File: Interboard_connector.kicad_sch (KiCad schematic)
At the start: 2 parts, among them J1 Chainbus Out, J4 Chainbus In

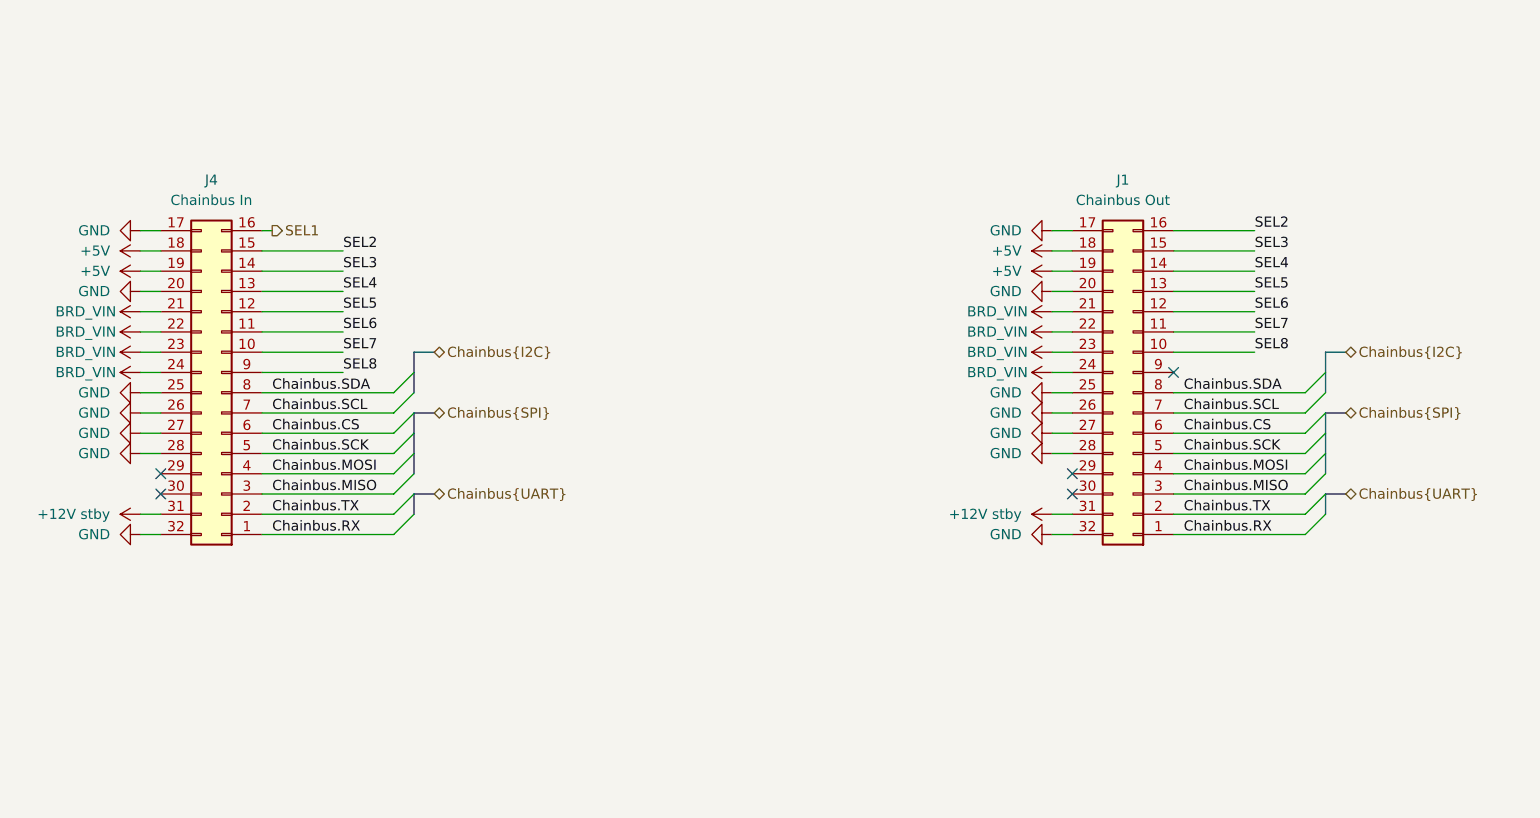
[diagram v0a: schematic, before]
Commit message: finished schematic (without some part numbers)
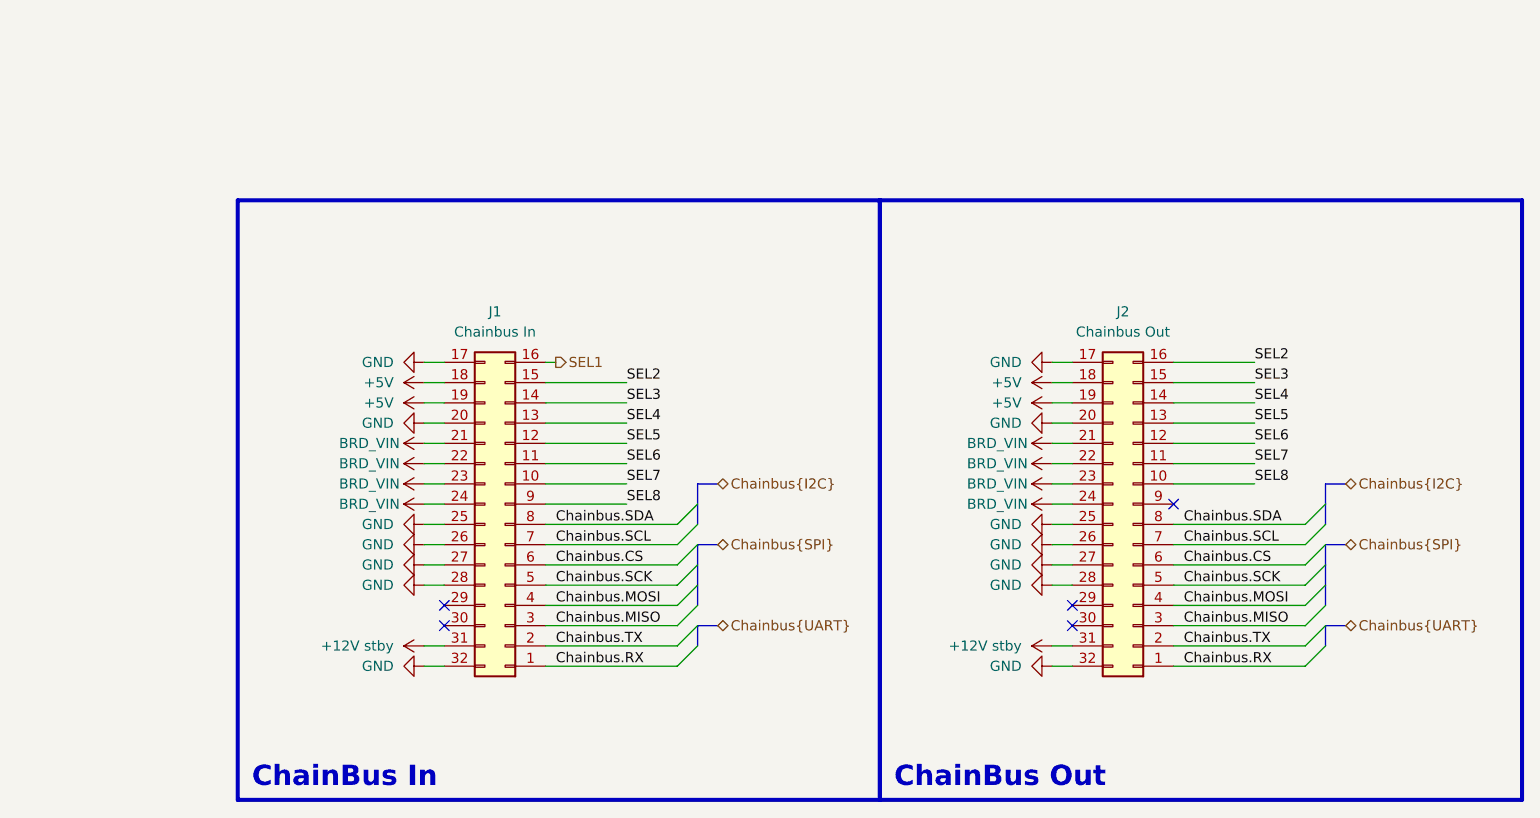
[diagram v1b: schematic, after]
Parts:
- renumbered J4 to J1, J1 to J2
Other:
- note added: "ChainBus In"
- note added: "ChainBus Out"
- moved on the sheet: J1, J2

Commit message: revision
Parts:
- removed J1: Chainbus In, Connector_PinSocket_2.54mm:PinSocket_2x16_P2.54mm_Vertical_SMD, symbol Connector_Generic:Conn_02x16_Counter_Clockwise
- removed J2: Chainbus Out, Connector_PinSocket_2.54mm:PinSocket_2x16_P2.54mm_Vertical_SMD, symbol Connector_Generic:Conn_02x16_Counter_Clockwise
- added J1: Chainbus in, Connector_PinSocket_2.54mm:PinSocket_2x16_P2.54mm_Vertical_SMD, symbol Connector_Generic:Conn_02x16_Odd_Even
- added J2: Chainbus Out, Connector_PinSocket_2.54mm:PinSocket_2x16_P2.54mm_Vertical_SMD, symbol Connector_Generic:Conn_02x16_Odd_Even
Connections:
- net +12V stby: now also J1.29 (Pin_29), J2.30 (Pin_30)
- net +5V: now also J1.3 (Pin_3), J1.5 (Pin_5), J2.4 (Pin_4), J2.6 (Pin_6)
- net BRD_VIN: now also J1.11 (Pin_11), J1.13 (Pin_13), J1.15 (Pin_15), J1.9 (Pin_9), J2.10 (Pin_10), J2.12 (Pin_12), J2.14 (Pin_14), J2.16 (Pin_16)
- net Chainbus.CS: now also J1.22 (Pin_22), J2.21 (Pin_21)
- net Chainbus.MISO: now also J1.28 (Pin_28), J2.27 (Pin_27)
- net Chainbus.MOSI: now also J1.26 (Pin_26), J2.25 (Pin_25)
- net Chainbus.RX: now also J1.32 (Pin_32), J2.31 (Pin_31)
- net Chainbus.SCK: now also J1.24 (Pin_24), J2.23 (Pin_23)
- net Chainbus.SCL: now also J1.20 (Pin_20), J2.19 (Pin_19)
- net Chainbus.SDA: now also J1.18 (Pin_18), J2.17 (Pin_17)
- net Chainbus.TX: now also J1.30 (Pin_30), J2.29 (Pin_29)
- net GND: now also J1.1 (Pin_1), J1.17 (Pin_17), J1.19 (Pin_19), J1.21 (Pin_21), J1.23 (Pin_23), J1.31 (Pin_31), J1.7 (Pin_7), J2.18 (Pin_18), J2.2 (Pin_2), J2.20 (Pin_20), J2.22 (Pin_22), J2.24 (Pin_24), J2.32 (Pin_32), J2.8 (Pin_8)
- net SEL1: now also J1.2 (Pin_2)
- net SEL2: now also J1.4 (Pin_4), J2.1 (Pin_1)
- net SEL3: now also J1.6 (Pin_6), J2.3 (Pin_3)
- net SEL4: now also J1.8 (Pin_8), J2.5 (Pin_5)
- net SEL5: now also J1.10 (Pin_10), J2.7 (Pin_7)
- net SEL6: now also J1.12 (Pin_12), J2.9 (Pin_9)
- net SEL7: now also J1.14 (Pin_14), J2.11 (Pin_11)
- net SEL8: now also J1.16 (Pin_16), J2.13 (Pin_13)

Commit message: second component placement
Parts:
- J1: footprint Connector_PinSocket_2.54mm:PinSocket_2x16_P2.54mm_Vertical_SMD -> Connector_PinHeader_2.54mm:PinHeader_2x16_P2.54mm_Vertical_SMD
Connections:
- net +12V stby: now also J2.29 (Pin_29); no longer J2.30 (Pin_30)
- net +5V: now also J2.3 (Pin_3), J2.5 (Pin_5); no longer J2.4 (Pin_4), J2.6 (Pin_6)
- net BRD_VIN: now also J2.11 (Pin_11), J2.13 (Pin_13), J2.15 (Pin_15), J2.9 (Pin_9); no longer J2.10 (Pin_10), J2.12 (Pin_12), J2.14 (Pin_14), J2.16 (Pin_16)
- net Chainbus.CS: now also J2.22 (Pin_22); no longer J2.21 (Pin_21)
- net Chainbus.MISO: now also J2.28 (Pin_28); no longer J2.27 (Pin_27)
- net Chainbus.MOSI: now also J2.26 (Pin_26); no longer J2.25 (Pin_25)
- net Chainbus.RX: now also J2.32 (Pin_32); no longer J2.31 (Pin_31)
- net Chainbus.SCK: now also J2.24 (Pin_24); no longer J2.23 (Pin_23)
- net Chainbus.SCL: now also J2.20 (Pin_20); no longer J2.19 (Pin_19)
- net Chainbus.SDA: now also J2.18 (Pin_18); no longer J2.17 (Pin_17)
- net Chainbus.TX: now also J2.30 (Pin_30); no longer J2.29 (Pin_29)
- net GND: now also J2.1 (Pin_1), J2.17 (Pin_17), J2.19 (Pin_19), J2.21 (Pin_21), J2.23 (Pin_23), J2.31 (Pin_31), J2.7 (Pin_7); no longer J2.18 (Pin_18), J2.2 (Pin_2), J2.20 (Pin_20), J2.22 (Pin_22), J2.24 (Pin_24), J2.32 (Pin_32), J2.8 (Pin_8)
- net SEL2: now also J2.2 (Pin_2); no longer J2.1 (Pin_1)
- net SEL3: now also J2.4 (Pin_4); no longer J2.3 (Pin_3)
- net SEL4: now also J2.6 (Pin_6); no longer J2.5 (Pin_5)
- net SEL5: now also J2.8 (Pin_8); no longer J2.7 (Pin_7)
- net SEL6: now also J2.10 (Pin_10); no longer J2.9 (Pin_9)
- net SEL7: now also J2.12 (Pin_12); no longer J2.11 (Pin_11)
- net SEL8: now also J2.14 (Pin_14); no longer J2.13 (Pin_13)
